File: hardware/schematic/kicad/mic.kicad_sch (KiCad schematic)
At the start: 64 parts, among them J501 NCJ6FI-S, SW501 +48V, U501 THAT1512S08, U502 OPA1612, U503 CS5361

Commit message: Add footprints and starting PCB so Altium import resolves every part
Altium's ECO reported "Footprint Not Found" for every part (and the
resulting "Unknown Pin" / class-member errors) because only KiCad
footprint names were included. Now:

- aio.kicad_pcb: every part placed with its footprint, all pads on their
  nets (unrouted), generated by pcb.py
- aio.pretty/: the 45 footprints the design uses, bundled with the project
- footprint fixes: five names that did not exist in the KiCad library
  replaced (coupled inductors -> two SRR1260 per converter, SRP5030T,
  RK097 dual pot, NCJ6FI-H, DPDT gain switch); parts without an explicit
  footprint now keep the symbol's default; phantom switch moved from a
  momentary push-button to a latching slide switch
- check.py also verifies every PCB pad's net against design.py
- README: Altium import steps (full project, then Make PCB Library)

U203 (XU316) still has no footprint: its pin numbers are placeholders
until the official XMOS library part replaces it.
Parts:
- D502, D503, D504, D505: footprint (none) -> Diode_THT:D_DO-41_SOD81_P10.16mm_Horizontal
- D508, D509: footprint (none) -> Package_TO_SOT_SMD:SOT-23
- J501: value NCJ6FI-S -> NCJ6FI-H; footprint Connector_Audio:Jack_XLR-6.35mm_Neutrik_NCJ6FI-S_Horizontal -> Connector_Audio:Jack_XLR-6.35mm_Neutrik_NCJ6FI-H_Horizontal; MPN NCJ6FI-S -> NCJ6FI-H
- SW501: footprint Button_Switch_THT:SW_PUSH_6mm -> Button_Switch_THT:SW_Slide_SPDT_Straight_CK_OS102011MS2Q
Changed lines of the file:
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@@
       )
     )
-    (property "Value" "NCJ6FI-S"
+    (property "Value" "NCJ6FI-H"
       (at 38.1 56.18 0)
       (effects
@@
       )
     )
-    (property "Footprint" "Connector_Audio:Jack_XLR-6.35mm_Neutrik_NCJ6FI-S_Horizontal"
+    (property "Footprint" "Connector_Audio:Jack_XLR-6.35mm_Neutrik_NCJ6FI-H_Horizontal"
       (at 38.1 35.56 0)
       (effects
@@
       )
     )
-    (property "MPN" "NCJ6FI-S"
+    (property "MPN" "NCJ6FI-H"
       (at 38.1 35.56 0)
       (effects
@@
       )
     )
-    (property "Value" "NCJ6FI-S"
+    (property "Value" "NCJ6FI-H"
       (at 65.41 42.64 0)
       (effects
@@
       )
     )
-    (property "Footprint" "Connector_Audio:Jack_XLR-6.35mm_Neutrik_NCJ6FI-S_Horizontal"
+    (property "Footprint" "Connector_Audio:Jack_XLR-6.35mm_Neutrik_NCJ6FI-H_Horizontal"
       (at 66.04 35.56 0)
       (effects
@@
       )
     )
-    (property "MPN" "NCJ6FI-S"
+    (property "MPN" "NCJ6FI-H"
       (at 66.04 35.56 0)
       (effects
@@
       )
     )
-    (property "Footprint" "Button_Switch_THT:SW_PUSH_6mm"
+    (property "Footprint" "Button_Switch_THT:SW_Slide_SPDT_Straight_CK_OS102011MS2Q"
       (at 226.06 33.02 0)
       (effects
@@
       )
     )
-    (property "Footprint" ""
+    (property "Footprint" "Diode_THT:D_DO-41_SOD81_P10.16mm_Horizontal"
       (at 198.12 68.58 0)
       (effects
@@
       )
     )
-    (property "Footprint" ""
+    (property "Footprint" "Diode_THT:D_DO-41_SOD81_P10.16mm_Horizontal"
       (at 226.06 68.58 0)
       (effects
@@
       )
     )
-    (property "Footprint" ""
+    (property "Footprint" "Diode_THT:D_DO-41_SOD81_P10.16mm_Horizontal"
       (at 256.54 68.58 0)
       (effects
@@
       )
     )
-    (property "Footprint" ""
+    (property "Footprint" "Diode_THT:D_DO-41_SOD81_P10.16mm_Horizontal"
       (at 284.48 68.58 0)
       (effects
@@
       )
     )
-    (property "Footprint" ""
+    (property "Footprint" "Package_TO_SOT_SMD:SOT-23"
       (at 340.36 134.62 0)
       (effects
@@
       )
     )
-    (property "Footprint" ""
+    (property "Footprint" "Package_TO_SOT_SMD:SOT-23"
       (at 375.92 134.62 0)
       (effects

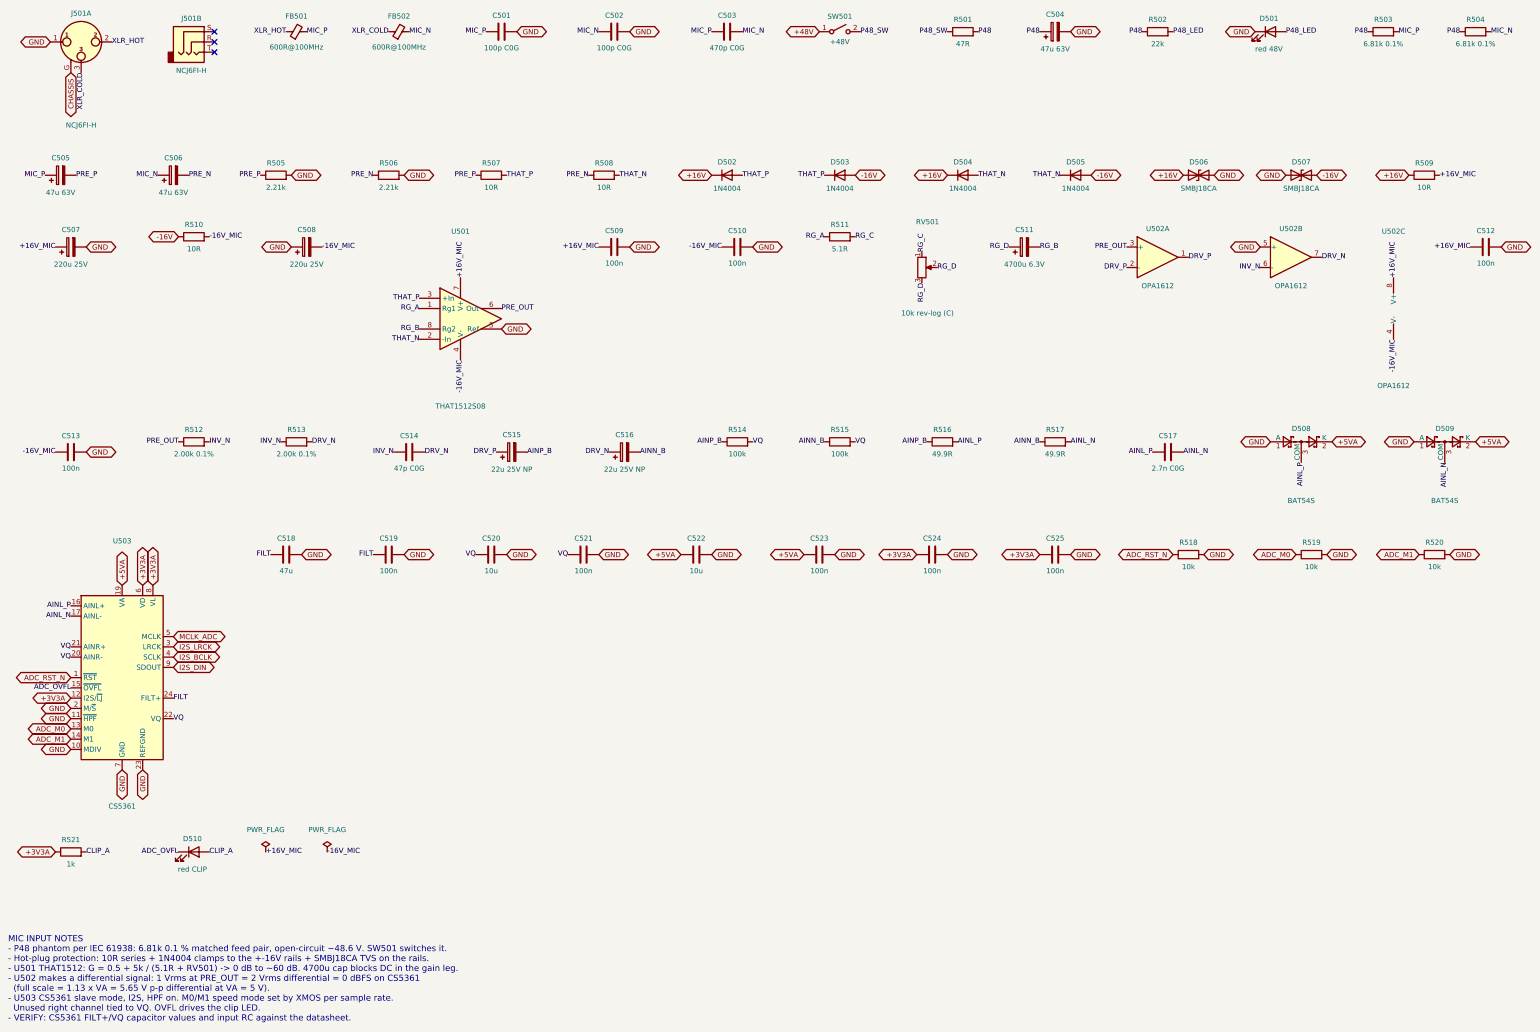
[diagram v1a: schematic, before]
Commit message: Split schematic into 14 A3 sheets, fix board outline, cluster placement
- Schematic: the five large A1/A0 sheets become 14 A3 sheets, one per
  function. Designators are unchanged (sections share one numbering
  sequence); the BOM is identical.
- PCB staging board: the outline was computed from board edges before any
  existed, so it came out far too small. It now encloses all parts. Parts
  are packed into one labelled cluster per sheet instead of one long strip.
- README: Altium steps for the "Missing child-sheet" errors (drop the top
  sheet, use global net scope) and layout guidance: don't autoroute the
  staging board.
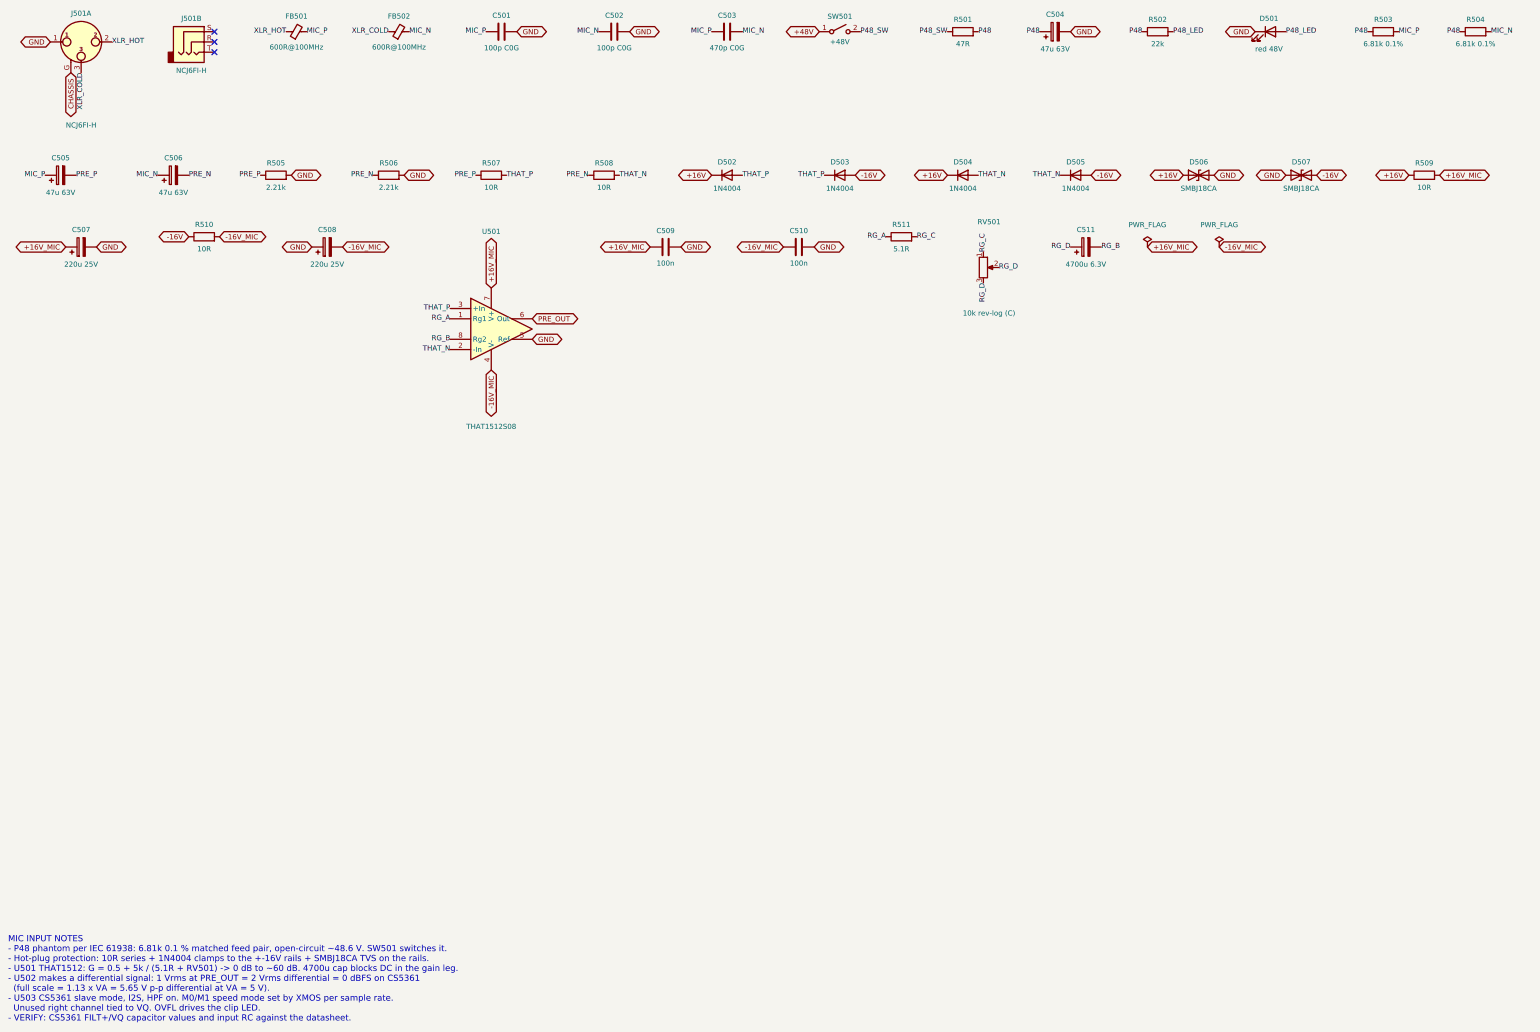
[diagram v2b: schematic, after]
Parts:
- removed C512, C513, C519, C521, C523, C524, C525: 100n, Capacitor_SMD:C_0603_1608Metric, symbol Device:C
- removed C514: 47p C0G, Capacitor_SMD:C_0603_1608Metric, symbol Device:C
- removed C515, C516: 22u 25V NP, Capacitor_SMD:CP_Elec_8x10, symbol Device:C_Polarized
- removed C517: 2.7n C0G, Capacitor_SMD:C_0603_1608Metric, symbol Device:C
- removed C518: 47u, Capacitor_SMD:C_1206_3216Metric, symbol Device:C
- removed C520, C522: 10u, Capacitor_SMD:C_0805_2012Metric, symbol Device:C
- removed D508, D509: BAT54S, Package_TO_SOT_SMD:SOT-23, symbol Diode:BAT54S
- removed D510: red CLIP, LED_SMD:LED_0805_2012Metric, symbol Device:LED
- removed R512, R513: 2.00k 0.1%, Resistor_SMD:R_0603_1608Metric, symbol Device:R
- removed R514, R515: 100k, Resistor_SMD:R_0603_1608Metric, symbol Device:R
- removed R516, R517: 49.9R, Resistor_SMD:R_0603_1608Metric, symbol Device:R
- removed R518, R519, R520: 10k, Resistor_SMD:R_0603_1608Metric, symbol Device:R
- removed R521: 1k, Resistor_SMD:R_0603_1608Metric, symbol Device:R
- removed U502: OPA1612, Package_SO:SOIC-8_3.9x4.9mm_P1.27mm, symbol Amplifier_Operational:OPA1612AxD
- removed U503: CS5361, Package_SO:TSSOP-24_4.4x7.8mm_P0.65mm, symbol Audio:CS5361
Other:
- title: Microphone input, phantom power, ADC -> Microphone input, phantom feed, preamp
- moved on the sheet: C507, C508, C509, C510, C511, R510, R511, RV501, U501
